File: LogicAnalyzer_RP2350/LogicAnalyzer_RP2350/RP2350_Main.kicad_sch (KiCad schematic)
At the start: 58 parts, among them J3 SM03B-SRSS-TB, SW1 SW_MEC_5G, SW2 SW_MEC_5G, U3 RP2350A, U4 W25Q128JVS, Y1 12Mhz

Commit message: Clearing UP ERC Errors and Warnings
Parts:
- added R47, R48, R49, R50: 33R, Resistor_SMD:R_0603_1608Metric_Pad0.98x0.95mm_HandSolder, symbol Device:R_Small
- J3: footprint CONN_SM03B-SRSS-TB_JST -> Connector_JST:JST_SH_SM03B-SRSS-TB_1x03-1MP_P1.00mm_Horizontal
- L3: footprint AOTAB201610S3R3101T -> ABRACON AOTA-B201610S3R3-101-T:AOTAB201610S3R3101T
- U3: footprint Package_DFN_QFN:QFN-60-1EP_7x7mm_P0.4mm_EP3.4x3.4mm -> Package_DFN_QFN:QFN-60-1EP_7x7mm_P0.4mm_EP3.4x3.4mm_ThermalVias; symbol MCU_RaspberryPi:RP2350A -> RP2350A_Abin:RP2350A
- U4: symbol Memory_Flash:W25Q128JVS -> Memory W25Q128JVS:W25Q128JVS_Abin
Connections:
- net D17: now also R47.2; no longer R35.2
- net D18: now also R48.2; no longer R36.2
- net D19: now also R49.2; no longer R37.2
- net D20: now also R50.2; no longer R38.2
- net QSPI_SCLK: now also U4.6 (CLK)
- net GP18: now reaches U3.29 (GPIO18)
- net GP18: now also R47.1
- net GP19: now reaches U3.31 (GPIO19)
- net GP19: now also R48.1
- net GP20: now reaches U3.32 (GPIO20)
- net GP20: now also R49.1
- net GP21: now reaches U3.33 (GPIO21)
- net GP21: now also R50.1
- new net D21: R35.2
- new net D22: R36.2
- new net D23: R37.2
- new net D24: R38.2
- no-connect marks 6 -> 2

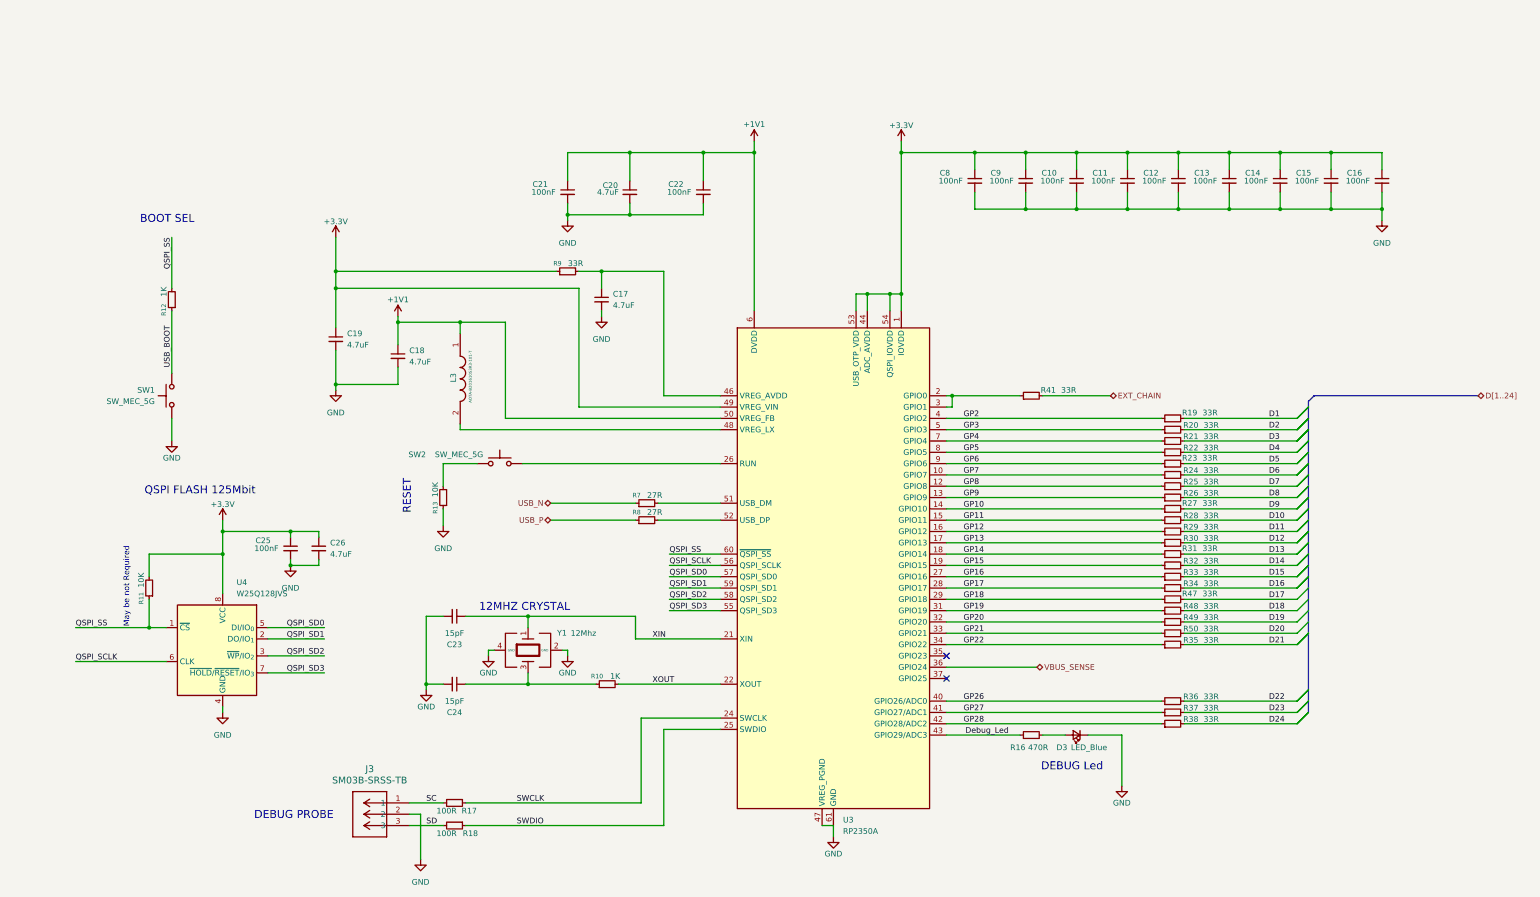
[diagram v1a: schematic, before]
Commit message: Net Classes Added
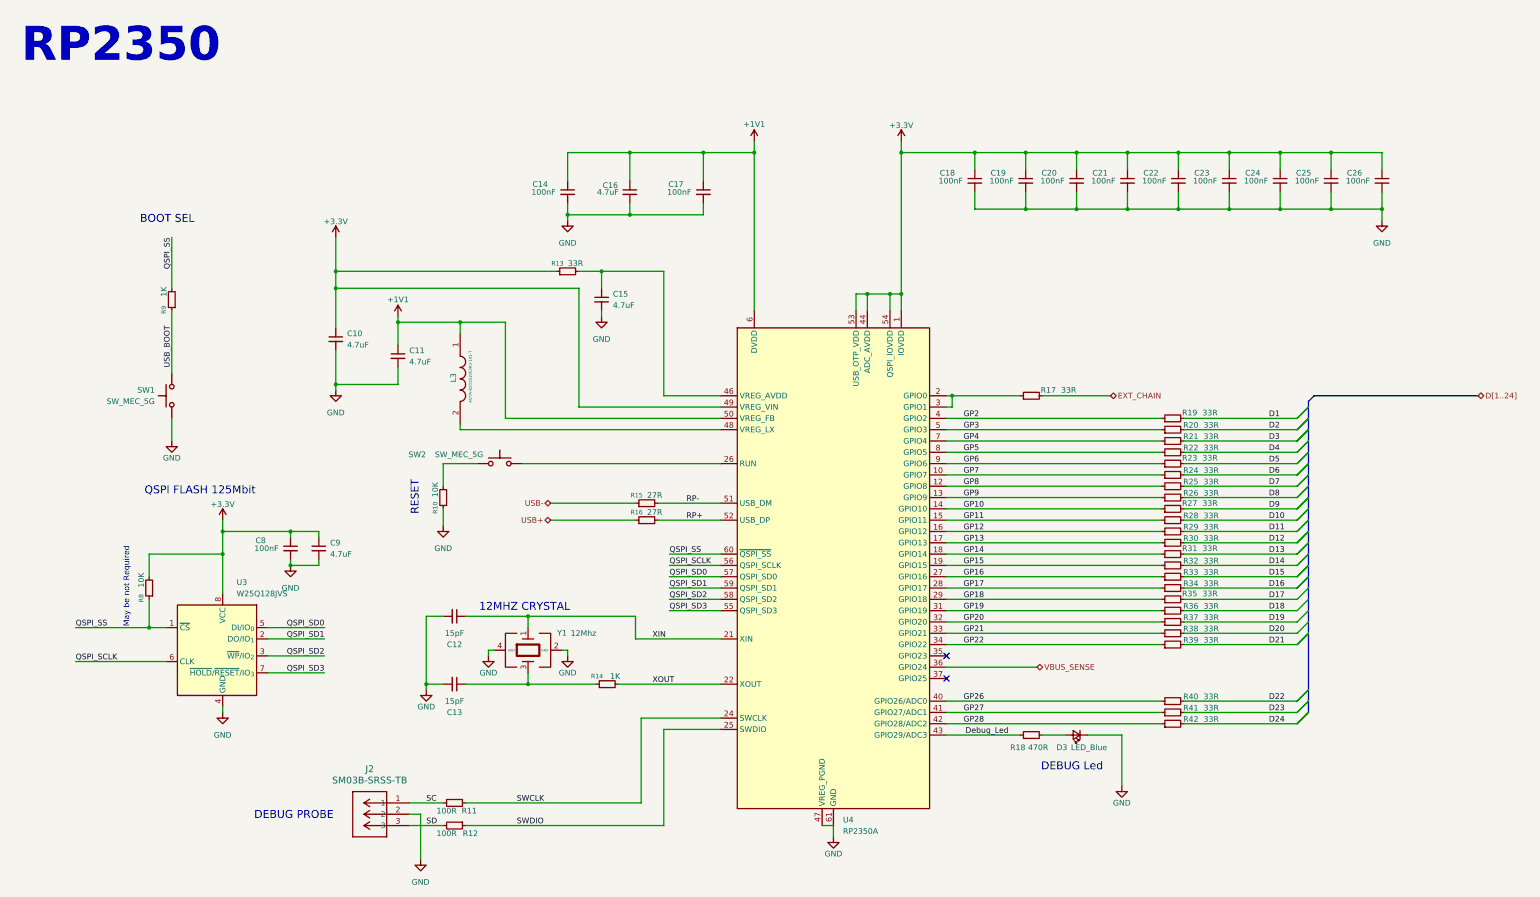
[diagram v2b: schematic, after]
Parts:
- renumbered C19 to C10, C18 to C11, C23 to C12, C24 to C13, C21 to C14, C17 to C15, C20 to C16, C22 to C17, C8 to C18, C9 to C19, C10 to C20, C11 to C21, C12 to C22, C13 to C23, C14 to C24, C15 to C25, C16 to C26, C25 to C8, C26 to C9, J3 to J2, R13 to R10, R17 to R11, R18 to R12, R9 to R13, R10 to R14, R7 to R15, R8 to R16, R41 to R17, R16 to R18, R47 to R35, R48 to R36, R49 to R37, R50 to R38, R35 to R39, R36 to R40, R37 to R41, R38 to R42, R11 to R8, R12 to R9, U4 to U3, U3 to U4
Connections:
- net RP+: now reaches R16.2, U4.52 (USB_DP)
- net RP-: now reaches R15.2, U4.51 (USB_DM)
- net USB_N renamed USB-
- net USB_P renamed USB+
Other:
- note added: "RP2350"
